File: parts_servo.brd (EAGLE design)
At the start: 33 x 16 mm, 43 parts, among them Q110 PMDPB28UN, Q120 PMDPB28UN, U1 MCP1703-3302, U100 RT9625A, U20 sn65hvd72, U50 nRF51822, X60 CX3225GB16000P0HPQCC

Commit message: Initial layout
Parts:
- moved R120 49.4 mm to (3.90, 3.60), turned to 0 degrees
- moved C120 48.3 mm to (6.00, 3.60), turned to 0 degrees
- moved JP3 47.7 mm to (12.7, 2.50), turned to 0 degrees
- moved Q120 44.7 mm to (8.30, 5.60), turned to 90 degrees
- moved C101 40.7 mm to (8.40, 8.70), turned to 0 degrees
- moved R122 39.4 mm to (8.70, 18.9), turned to 270 degrees
- moved R111 39.0 mm to (13.6, 14.2), turned to 0 degrees
- moved R121 38.0 mm to (8.00, 10.9), turned to 0 degrees
- moved Q110 37.5 mm to (23.5, 10.2), turned to 0 degrees
- moved C100 36.8 mm to (20.8, 10.2), turned to 270 degrees
- moved R112 35.8 mm to (18.1, 10.7), turned to 270 degrees
- moved C102 31.4 mm to (11.1, 14.1), turned to 0 degrees
- moved C110 30.9 mm to (22.0, 14.5), turned to 270 degrees
- moved R102 29.5 mm to (12.1, 11.9), turned to 0 degrees
- moved R110 28.0 mm to (21.9, 16.7), turned to 270 degrees
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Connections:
- removed net SENSOR7: JP2.7, U50.7
- new net SENSOR2: JP2.3, U50.6
- net DIFFERENTIAL_INPUT: now also U50.48; no longer U50.40
- net DIFFERENTIAL_INPUT_EN: now also U50.47; no longer U50.27
- net DIFFERENTIAL_OUTPUT: now also U50.43; no longer U50.28
- net DIFFERENTIAL_OUTPUT_EN: now also U50.44; no longer U50.26
- net PWM1: now also U50.15; no longer U50.14
- net PWM2: now also U50.18; no longer U50.15
- net PWM_POR: now also U50.14; no longer U50.18
- net SENSOR3: now also JP2.4; no longer JP2.3
- net SENSOR4: now also JP2.5, U50.8; no longer JP2.4, U50.9
- net SENSOR5: now also JP2.6, U50.7; no longer JP2.5, U50.6
- net SENSOR6: now also JP2.7, U50.9; no longer JP2.6, U50.8
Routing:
- net GND: track 0.00 -> 169.3 mm, vias 0 -> 1
- net POWER_IN: track 0.00 -> 82.6 mm, vias 0 -> 2
- net MOTOR2: track 0.00 -> 39.2 mm, vias 0 -> 2
- net 3.3V: track 0.00 -> 31.0 mm
- net UNIPOLAR_OUTPUT: track 0.00 -> 30.8 mm
- net MOTOR1: track 0.00 -> 30.6 mm, vias 0 -> 1
- net BOOT1: track 0.00 -> 22.5 mm
- net UNIPOLAR_INPUT: track 0.00 -> 21.7 mm, vias 0 -> 2
- net D1/TX: track 0.00 -> 20.2 mm
- net QUGATE1: track 0.00 -> 17.2 mm
- net QLGATE2: track 0.00 -> 13.5 mm
- net D2/RX: track 0.00 -> 10.8 mm
- net LGATE1: track 0.00 -> 9.18 mm
- net SENSOR1: track 0.00 -> 8.67 mm
- net SENSOR6: track 0.00 -> 8.50 mm
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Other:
- board size 33 x 16 mm -> 38.7 x 49.8 mm

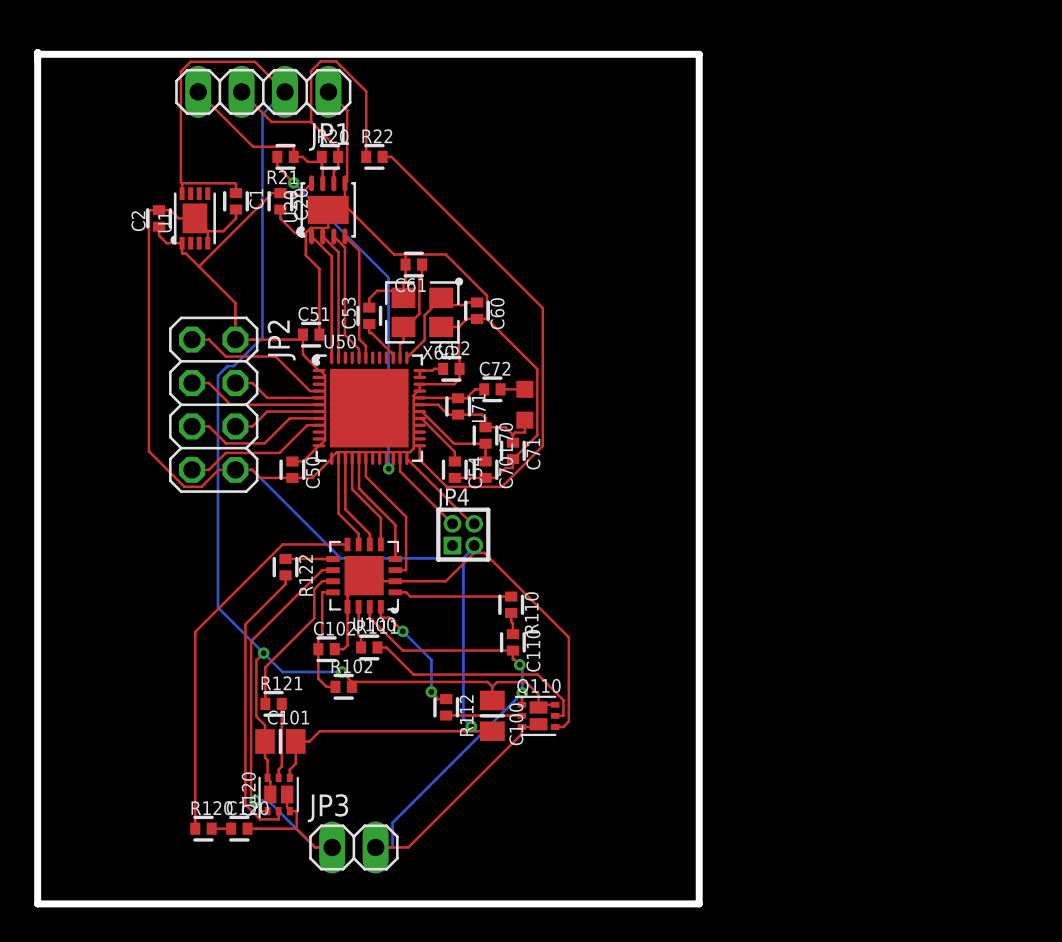
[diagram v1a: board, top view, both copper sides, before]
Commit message: Removed all the DRC errors.
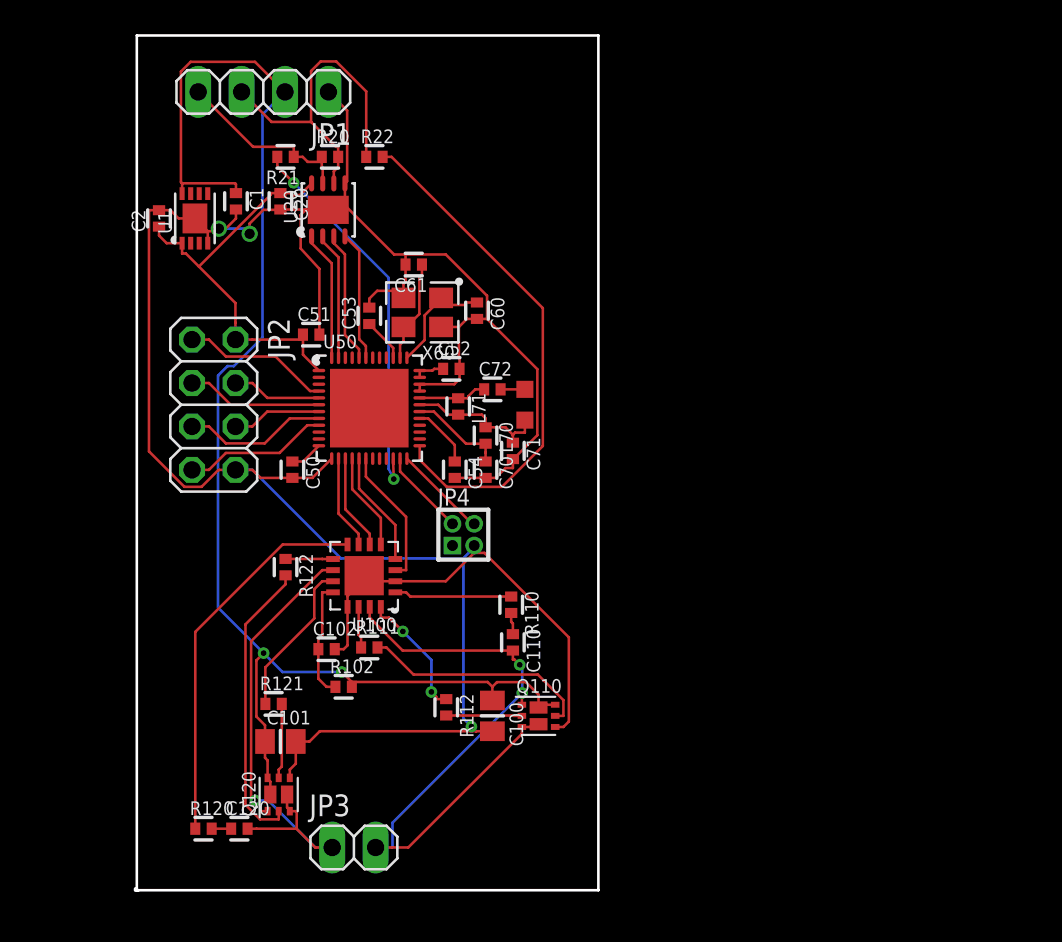
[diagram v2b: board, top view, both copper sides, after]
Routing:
- net 3.3V: track 31.0 -> 26.4 mm
- net GND: track 169.3 -> 165.2 mm, vias 1 -> 3
- net UNIPOLAR_INPUT: track 21.7 -> 22.8 mm
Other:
- board size 38.7 x 49.8 mm -> 27.1 x 50 mm
